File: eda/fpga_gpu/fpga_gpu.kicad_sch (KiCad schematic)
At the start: 36 parts, among them J3 programming, J4 reset ground, Q1 2N7002, SW1 SW_Reset, SW2 SW_FlashPwrCycle, U1 ICE40HX4K-TQ144, U10 IS61C5128AL-10KLI, U2 SST25VF080B-50-4x-S2Ax, U8 AMS1117-3.3, U9 AP2112K-1.2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

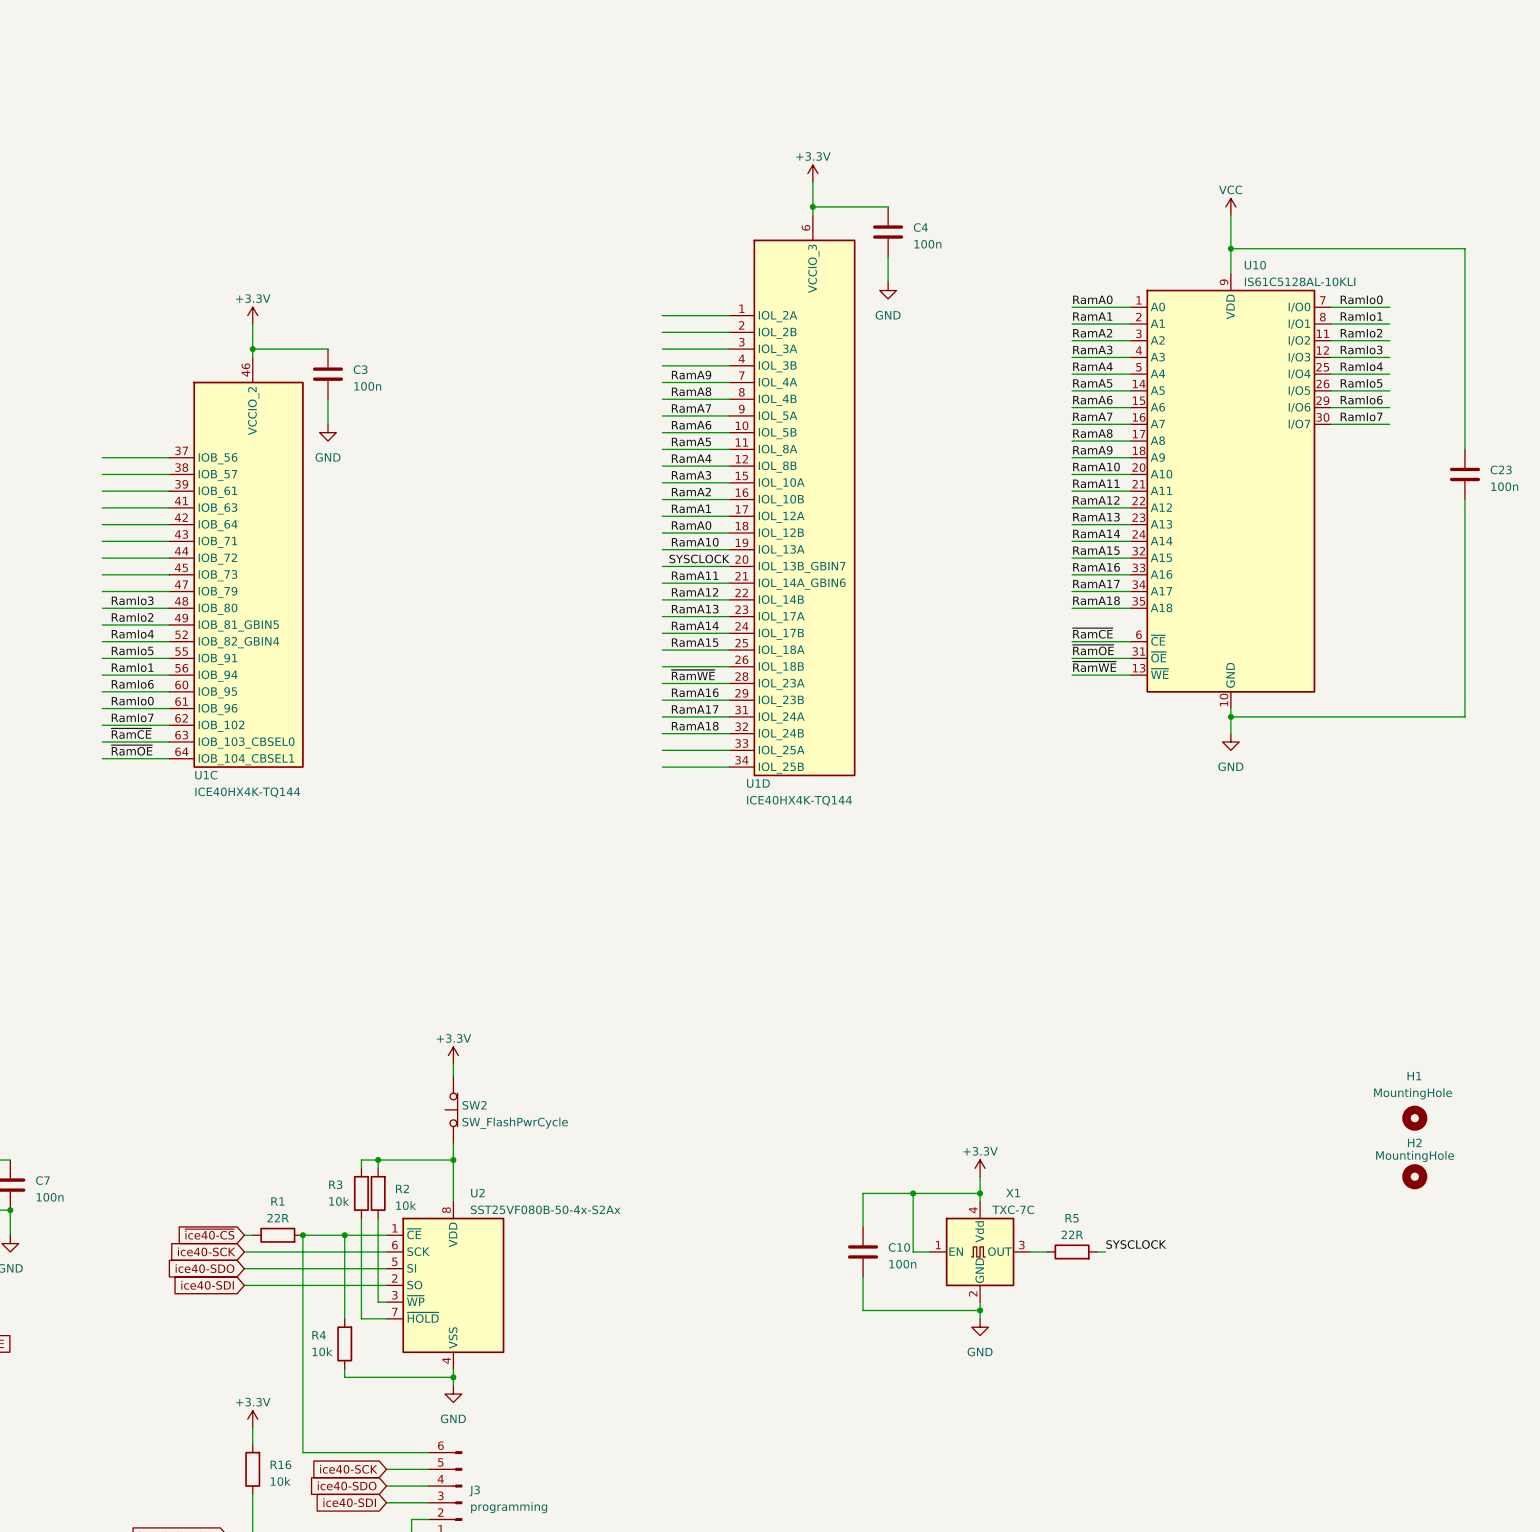
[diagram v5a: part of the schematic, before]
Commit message: Generate step files and start on gpu for new board layout
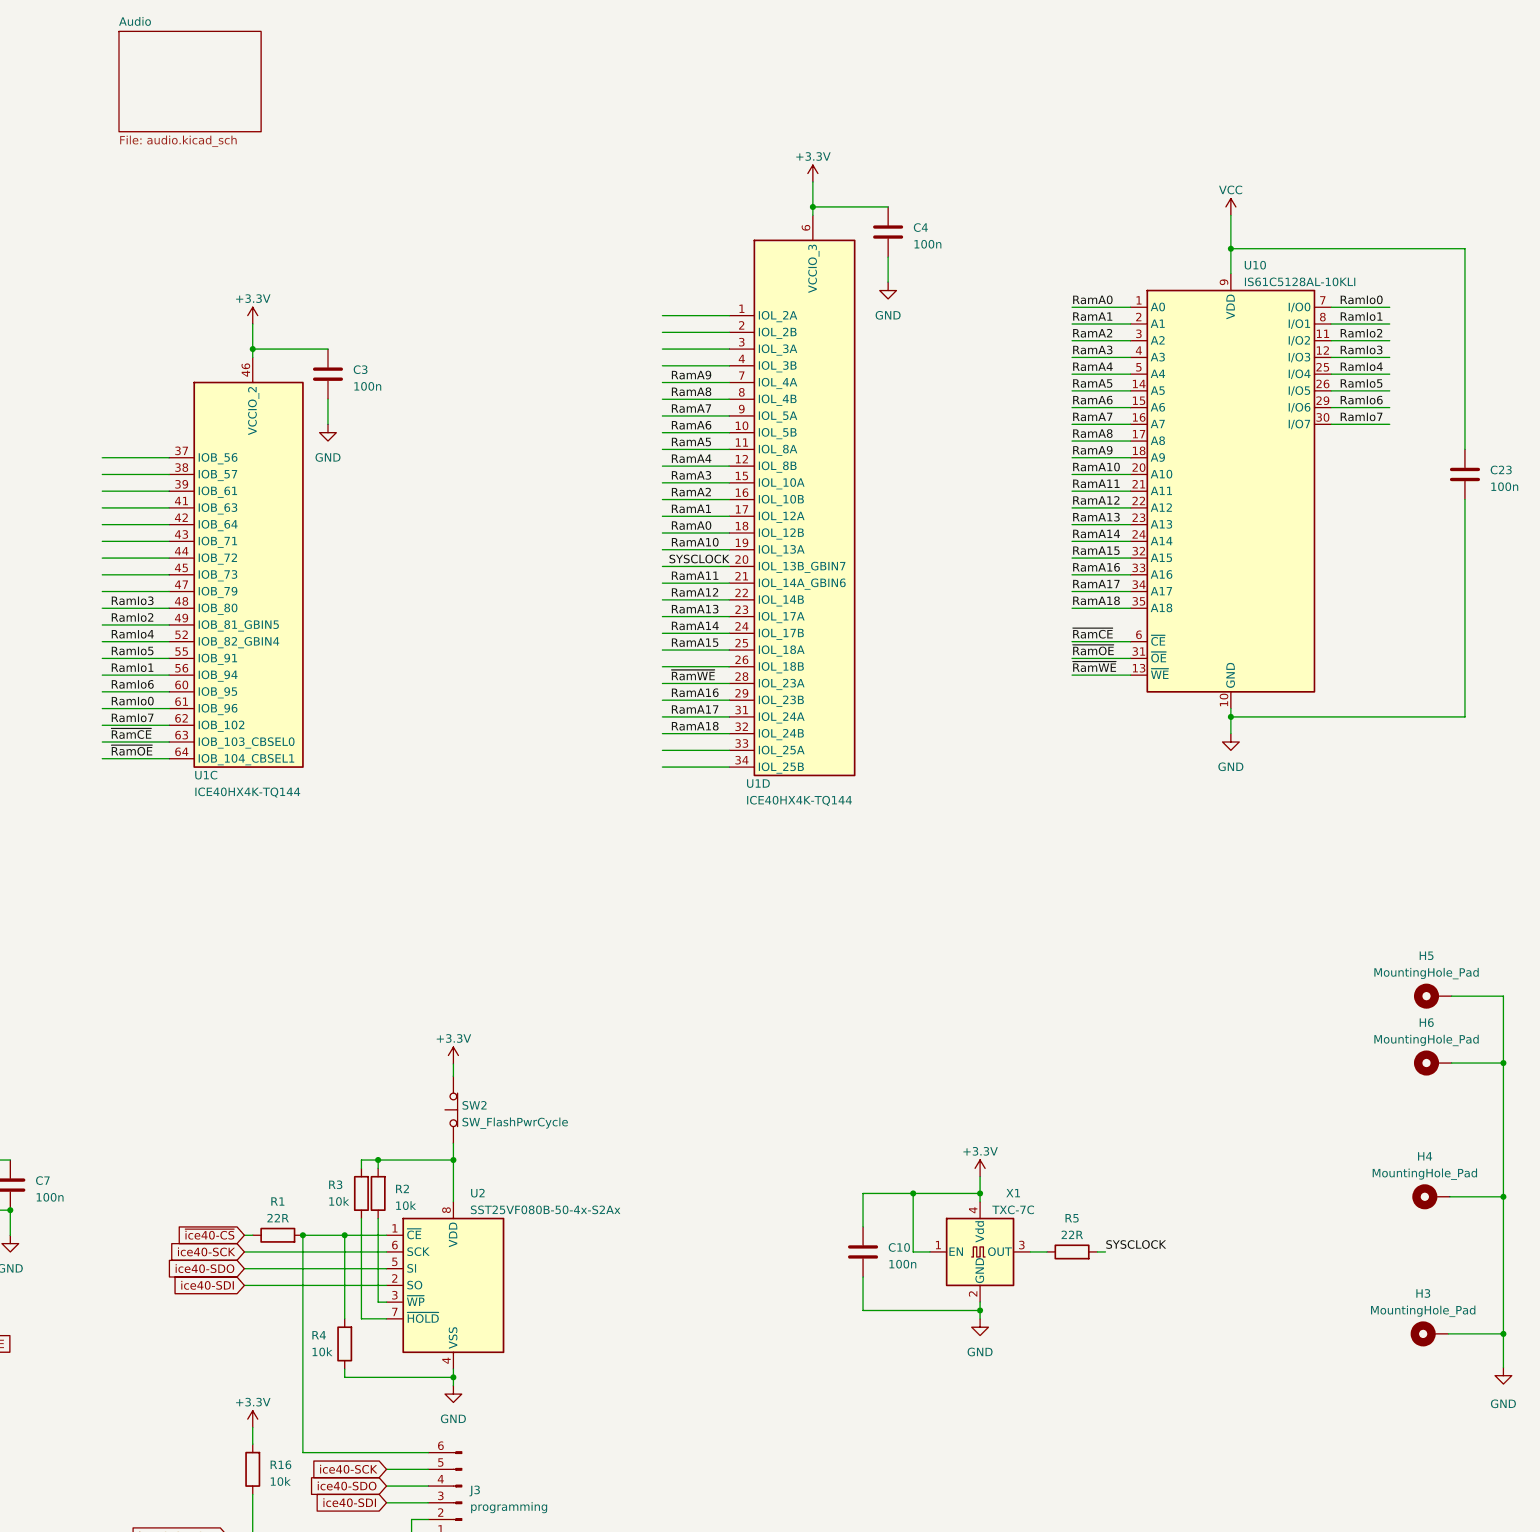
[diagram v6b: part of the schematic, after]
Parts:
- removed H1, H2: MountingHole, MountingHole:MountingHole_2.5mm, symbol Mechanical:MountingHole
- added H3, H4, H5, H6: MountingHole_Pad, MountingHole:MountingHole_2.5mm_Pad_Via, symbol Mechanical:MountingHole_Pad
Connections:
- net GND: now also H3.1, H4.1, H5.1, H6.1
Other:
- added sheet Audio (audio.kicad_sch)
